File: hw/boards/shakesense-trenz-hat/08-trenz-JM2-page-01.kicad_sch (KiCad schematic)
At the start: 1 part, among them J81 LSHM-150-04.0-L-DV-A-S-K-TR

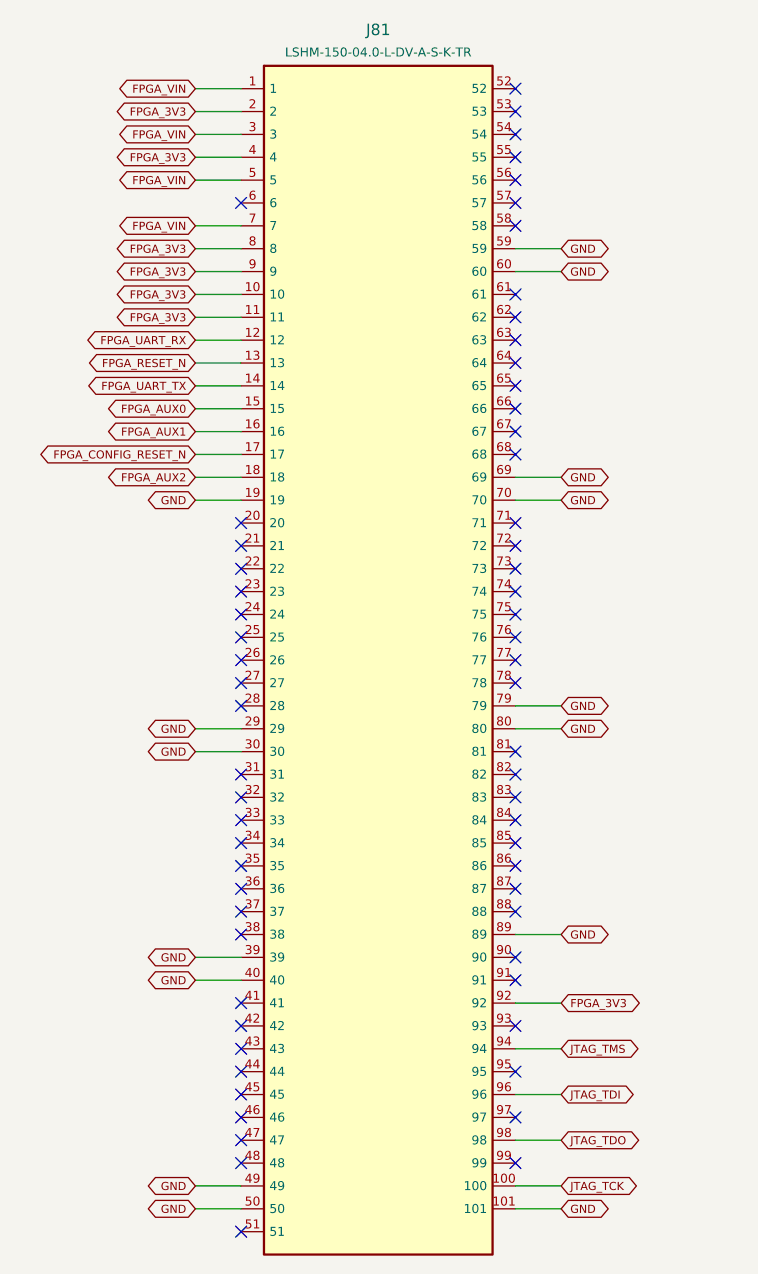
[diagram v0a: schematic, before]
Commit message: Expose Trenz GPIOs on the Pi-outline HDI sensor HAT
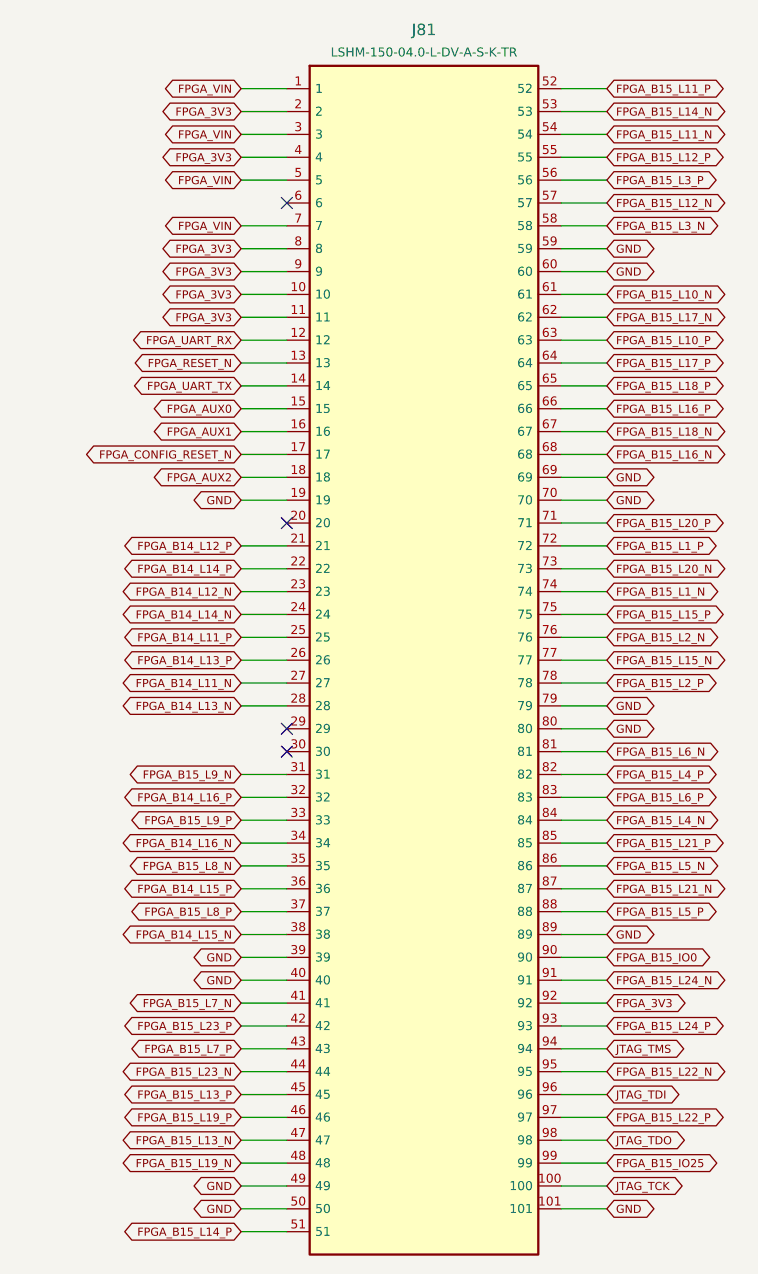
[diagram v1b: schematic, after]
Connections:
- net GND: no longer J81.29, J81.30
- net FPGA_B14_L12_P: now reaches J81.21
- net FPGA_B14_L14_P: now reaches J81.22
- net FPGA_B14_L12_N: now reaches J81.23
- net FPGA_B14_L14_N: now reaches J81.24
- net FPGA_B14_L11_P: now reaches J81.25
- net FPGA_B14_L13_P: now reaches J81.26
- net FPGA_B14_L11_N: now reaches J81.27
- net FPGA_B14_L13_N: now reaches J81.28
- net FPGA_B15_L9_N: now reaches J81.31
- net FPGA_B14_L16_P: now reaches J81.32
- net FPGA_B15_L9_P: now reaches J81.33
- net FPGA_B14_L16_N: now reaches J81.34
- net FPGA_B15_L8_N: now reaches J81.35
- net FPGA_B14_L15_P: now reaches J81.36
- net FPGA_B15_L8_P: now reaches J81.37
- net FPGA_B14_L15_N: now reaches J81.38
- net FPGA_B15_L7_N: now reaches J81.41
- net FPGA_B15_L23_P: now reaches J81.42
- net FPGA_B15_L7_P: now reaches J81.43
- net FPGA_B15_L23_N: now reaches J81.44
- net FPGA_B15_L13_P: now reaches J81.45
- net FPGA_B15_L19_P: now reaches J81.46
- net FPGA_B15_L13_N: now reaches J81.47
- net FPGA_B15_L19_N: now reaches J81.48
- net FPGA_B15_L14_P: now reaches J81.51
- net FPGA_B15_L11_P: now reaches J81.52
- net FPGA_B15_L14_N: now reaches J81.53
- net FPGA_B15_L11_N: now reaches J81.54
- net FPGA_B15_L12_P: now reaches J81.55
- net FPGA_B15_L3_P: now reaches J81.56
- net FPGA_B15_L12_N: now reaches J81.57
- net FPGA_B15_L3_N: now reaches J81.58
- net FPGA_B15_L10_N: now reaches J81.61
- net FPGA_B15_L17_N: now reaches J81.62
- net FPGA_B15_L10_P: now reaches J81.63
- net FPGA_B15_L17_P: now reaches J81.64
- net FPGA_B15_L18_P: now reaches J81.65
- net FPGA_B15_L16_P: now reaches J81.66
- net FPGA_B15_L18_N: now reaches J81.67
- net FPGA_B15_L16_N: now reaches J81.68
- net FPGA_B15_L20_P: now reaches J81.71
- net FPGA_B15_L1_P: now reaches J81.72
- net FPGA_B15_L20_N: now reaches J81.73
- net FPGA_B15_L1_N: now reaches J81.74
- net FPGA_B15_L15_P: now reaches J81.75
- net FPGA_B15_L2_N: now reaches J81.76
- net FPGA_B15_L15_N: now reaches J81.77
- net FPGA_B15_L2_P: now reaches J81.78
- net FPGA_B15_L6_N: now reaches J81.81
- net FPGA_B15_L4_P: now reaches J81.82
- net FPGA_B15_L6_P: now reaches J81.83
- net FPGA_B15_L4_N: now reaches J81.84
- net FPGA_B15_L21_P: now reaches J81.85
- net FPGA_B15_L5_N: now reaches J81.86
- net FPGA_B15_L21_N: now reaches J81.87
- net FPGA_B15_L5_P: now reaches J81.88
- net FPGA_B15_IO0: now reaches J81.90
- net FPGA_B15_L24_N: now reaches J81.91
- net FPGA_B15_L24_P: now reaches J81.93
- net FPGA_B15_L22_N: now reaches J81.95
- net FPGA_B15_L22_P: now reaches J81.97
- net FPGA_B15_IO25: now reaches J81.99
- no-connect marks 64 -> 4
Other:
- title: shakesense-trenz-hat / 08-trenz-JM2-page-01 -> ShakeSense T1 / 08-trenz-JM2-page-01
- moved on the sheet: J81

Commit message: Implement internal Pi FPGA link and remove ribbon expansion
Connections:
- net FPGA_AUX0: no longer names the net of J81.15
- net FPGA_AUX1: no longer names the net of J81.16
- net FPGA_AUX2: no longer names the net of J81.18
- net FPGA_B14_L11_N: no longer names the net of J81.27
- net FPGA_B14_L11_P: no longer names the net of J81.25
- net FPGA_B14_L12_N renamed FPGA_LINK_CS_N
- net FPGA_B14_L12_P renamed FPGA_LINK_SCLK
- net FPGA_B14_L13_N renamed FPGA_LINK_DQ3
- net FPGA_B14_L13_P renamed FPGA_LINK_DQ2
- net FPGA_B14_L14_N renamed FPGA_LINK_DQ1
- net FPGA_B14_L14_P renamed FPGA_LINK_DQ0
- net FPGA_B14_L15_N: no longer names the net of J81.38
- net FPGA_B14_L15_P: no longer names the net of J81.36
- net FPGA_B14_L16_N: no longer names the net of J81.34
- net FPGA_B14_L16_P: no longer names the net of J81.32
- net FPGA_B15_IO0: no longer names the net of J81.90
- net FPGA_B15_IO25: no longer names the net of J81.99
- net FPGA_B15_L10_N: no longer names the net of J81.61
- net FPGA_B15_L10_P: no longer names the net of J81.63
- net FPGA_B15_L11_N: no longer names the net of J81.54
- net FPGA_B15_L11_P: no longer names the net of J81.52
- net FPGA_B15_L12_N: no longer names the net of J81.57
- net FPGA_B15_L12_P: no longer names the net of J81.55
- net FPGA_B15_L13_N: no longer names the net of J81.47
- net FPGA_B15_L13_P: no longer names the net of J81.45
- net FPGA_B15_L14_N: no longer names the net of J81.53
- net FPGA_B15_L14_P: no longer names the net of J81.51
- net FPGA_B15_L15_N: no longer names the net of J81.77
- net FPGA_B15_L15_P: no longer names the net of J81.75
- net FPGA_B15_L16_N: no longer names the net of J81.68
- net FPGA_B15_L16_P: no longer names the net of J81.66
- net FPGA_B15_L17_N: no longer names the net of J81.62
- net FPGA_B15_L17_P: no longer names the net of J81.64
- net FPGA_B15_L18_N: no longer names the net of J81.67
- net FPGA_B15_L18_P: no longer names the net of J81.65
- net FPGA_B15_L19_N: no longer names the net of J81.48
- net FPGA_B15_L19_P: no longer names the net of J81.46
- net FPGA_B15_L1_N: no longer names the net of J81.74
- net FPGA_B15_L1_P: no longer names the net of J81.72
- net FPGA_B15_L20_N: no longer names the net of J81.73
- net FPGA_B15_L20_P: no longer names the net of J81.71
- net FPGA_B15_L21_N: no longer names the net of J81.87
- net FPGA_B15_L21_P: no longer names the net of J81.85
- net FPGA_B15_L22_N: no longer names the net of J81.95
- net FPGA_B15_L22_P: no longer names the net of J81.97
- net FPGA_B15_L23_N: no longer names the net of J81.44
- net FPGA_B15_L23_P: no longer names the net of J81.42
- net FPGA_B15_L24_N: no longer names the net of J81.91
- net FPGA_B15_L24_P: no longer names the net of J81.93
- net FPGA_B15_L2_N: no longer names the net of J81.76
- net FPGA_B15_L2_P: no longer names the net of J81.78
- net FPGA_B15_L3_N: no longer names the net of J81.58
- net FPGA_B15_L3_P: no longer names the net of J81.56
- net FPGA_B15_L4_N: no longer names the net of J81.84
- net FPGA_B15_L4_P: no longer names the net of J81.82
- net FPGA_B15_L5_N: no longer names the net of J81.86
- net FPGA_B15_L5_P: no longer names the net of J81.88
- net FPGA_B15_L6_N: no longer names the net of J81.81
- net FPGA_B15_L6_P: no longer names the net of J81.83
- net FPGA_B15_L7_N: no longer names the net of J81.41
- net FPGA_B15_L7_P: no longer names the net of J81.43
- net FPGA_B15_L8_N: no longer names the net of J81.35
- net FPGA_B15_L8_P: no longer names the net of J81.37
- net FPGA_B15_L9_N: no longer names the net of J81.31
- net FPGA_B15_L9_P: no longer names the net of J81.33
- no-connect marks 4 -> 63
